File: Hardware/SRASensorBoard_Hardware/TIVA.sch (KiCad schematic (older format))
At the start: 7 parts, among them U4 TM4C129E_Launchpad

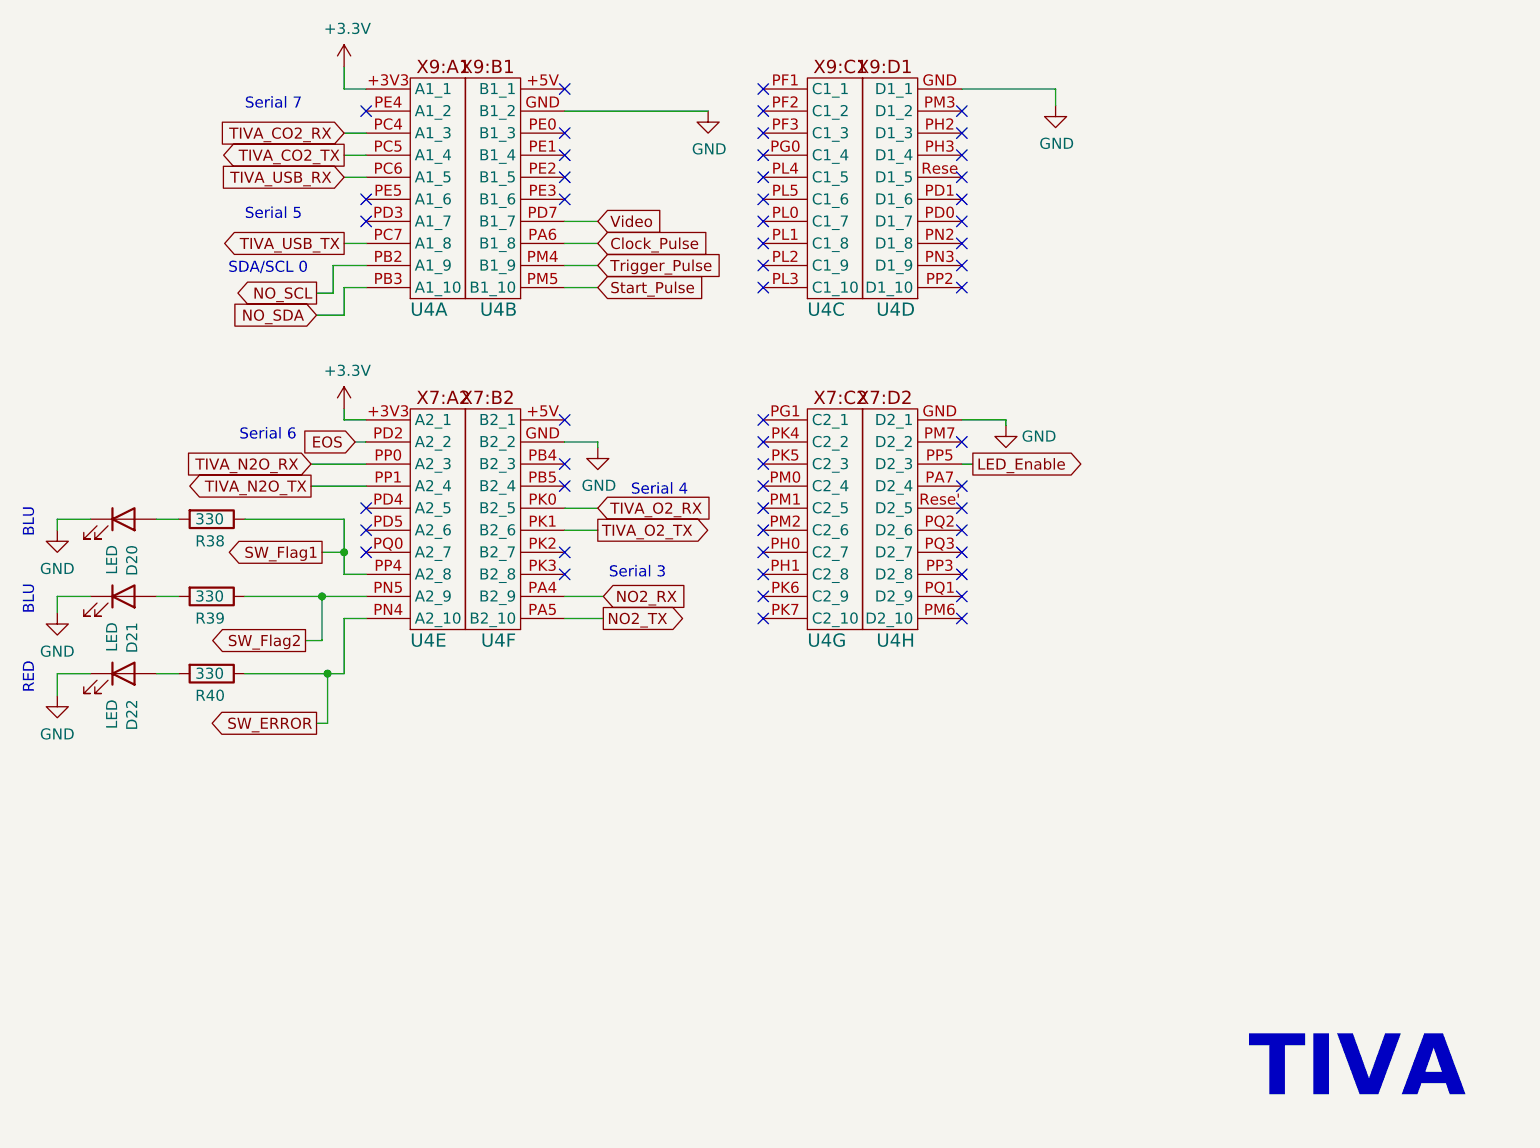
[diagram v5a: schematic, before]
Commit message: Board Progress 3
New mosfets are in but old mosfets need some clean up
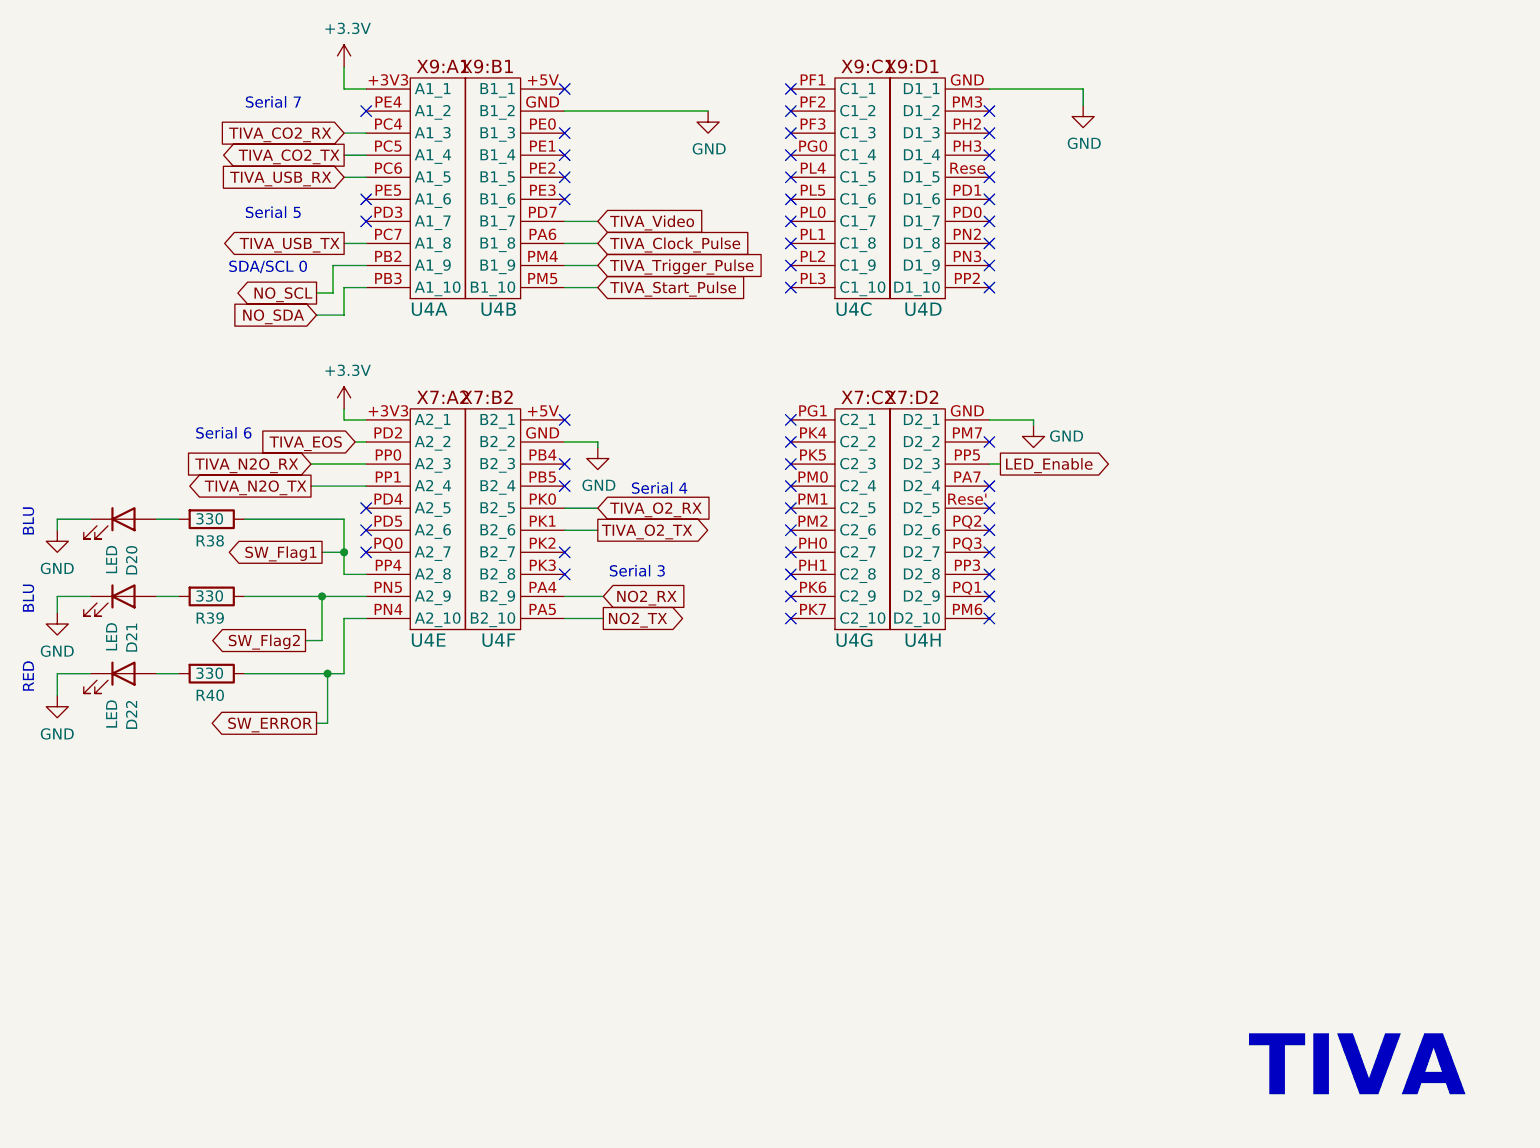
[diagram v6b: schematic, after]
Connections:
- net Clock_Pulse renamed TIVA_Clock_Pulse
- net EOS renamed TIVA_EOS
- net Start_Pulse renamed TIVA_Start_Pulse
- net Trigger_Pulse renamed TIVA_Trigger_Pulse
- net Video renamed TIVA_Video
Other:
- moved on the sheet: U4C, U4D, U4G, U4H
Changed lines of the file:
@@
 TIVA\n
 Wire Wire Line
-	7150 4100 7100 4100
-Text GLabel 7150 4100 2    50   Output ~ 0
+	7275 4100 7225 4100
+Text GLabel 7275 4100 2    50   Output ~ 0
 LED_Enable
 Text GLabel 4175 5275 0    50   Output ~ 0
@@
 L power:GND #PWR0167
 U 1 1 5F933A36
-P 7525 2475
-F 0 "#PWR0167" H 7525 2225 50  0001 C CNN
-F 1 "GND" H 7530 2302 50  0000 C CNN
-F 2 "" H 7525 2475 50  0001 C CNN
-F 3 "" H 7525 2475 50  0001 C CNN
-	1    7525 2475
+P 7650 2475
+F 0 "#PWR0167" H 7650 2225 50  0001 C CNN
+F 1 "GND" H 7655 2302 50  0000 C CNN
+F 2 "" H 7650 2475 50  0001 C CNN
+F 3 "" H 7650 2475 50  0001 C CNN
+	1    7650 2475
 	1    0    0    -1
 $EndComp
@@
 NoConn ~ 5300 4200
 NoConn ~ 5300 4500
-NoConn ~ 6200 4800
-NoConn ~ 6200 4700
-NoConn ~ 6200 4600
-NoConn ~ 6200 4500
-NoConn ~ 6200 4400
-NoConn ~ 6200 4300
-NoConn ~ 6200 4200
-NoConn ~ 6200 4100
-NoConn ~ 7100 4200
-NoConn ~ 7100 4400
-NoConn ~ 7100 4500
-NoConn ~ 7100 4600
-NoConn ~ 7100 4700
-NoConn ~ 7100 4800
-NoConn ~ 7100 3300
-NoConn ~ 7100 3200
-NoConn ~ 7100 3100
-NoConn ~ 7100 3000
-NoConn ~ 7100 2900
-NoConn ~ 7100 2800
-NoConn ~ 7100 2700
-NoConn ~ 7100 2600
-NoConn ~ 6200 2400
-NoConn ~ 6200 2500
-NoConn ~ 6200 2600
-NoConn ~ 6200 2700
-NoConn ~ 6200 2800
-NoConn ~ 6200 2900
-NoConn ~ 6200 3000
-NoConn ~ 6200 3100
-NoConn ~ 6200 3200
-NoConn ~ 6200 3300
+NoConn ~ 6325 4800
+NoConn ~ 6325 4700
+NoConn ~ 6325 4600
+NoConn ~ 6325 4500
+NoConn ~ 6325 4400
+NoConn ~ 6325 4300
+NoConn ~ 6325 4200
+NoConn ~ 6325 4100
+NoConn ~ 7225 4200
+NoConn ~ 7225 4400
+NoConn ~ 7225 4500
+NoConn ~ 7225 4600
+NoConn ~ 7225 4700
+NoConn ~ 7225 4800
+NoConn ~ 7225 3300
+NoConn ~ 7225 3200
+NoConn ~ 7225 3100
+NoConn ~ 7225 3000
+NoConn ~ 7225 2900
+NoConn ~ 7225 2800
+NoConn ~ 7225 2700
+NoConn ~ 7225 2600
+NoConn ~ 6325 2400
+NoConn ~ 6325 2500
+NoConn ~ 6325 2600
+NoConn ~ 6325 2700
+NoConn ~ 6325 2800
+NoConn ~ 6325 2900
+NoConn ~ 6325 3000
+NoConn ~ 6325 3100
+NoConn ~ 6325 3200
+NoConn ~ 6325 3300
 NoConn ~ 4400 3000
 NoConn ~ 4400 2500
 NoConn ~ 5300 2900
-NoConn ~ 7100 4300
+NoConn ~ 7225 4300
 $Comp
 L power:+3.3V #PWR0170
@@
 L SRA_Sensor_Board-rescue:TM4C129E_Launchpad-MRDT_Shields-SRA_Sensor_Board-rescue U4
 U 3 1 5F933A94
-P 6400 3350
-F 0 "U4" H 6400 3300 60  0000 L CNN
-F 1 "TM4C129E_Launchpad" H 6150 3300 60  0001 L CNN
-F 2 "MRDT_Shields:TM4C129E_Launchpad_FULL_SMD_BOTTOM" H 6400 3350 60  0001 C CNN
-F 3 "" H 6400 3350 60  0001 C CNN
-	3    6400 3350
+P 6525 3350
+F 0 "U4" H 6525 3300 60  0000 L CNN
+F 1 "TM4C129E_Launchpad" H 6275 3300 60  0001 L CNN
+F 2 "MRDT_Shields:TM4C129E_Launchpad_FULL_SMD_BOTTOM" H 6525 3350 60  0001 C CNN
+F 3 "" H 6525 3350 60  0001 C CNN
+	3    6525 3350
 	1    0    0    -1
 $EndComp
@@
 L SRA_Sensor_Board-rescue:TM4C129E_Launchpad-MRDT_Shields-SRA_Sensor_Board-rescue U4
 U 8 1 5F933ACF
-P 6900 4850
-F 0 "U4" H 7000 4800 60  0000 C CNN
-F 1 "TM4C129E_Launchpad" H 7150 4800 60  0001 C CNN
-F 2 "MRDT_Shields:TM4C129E_Launchpad_FULL_SMD_BOTTOM" H 6900 4850 60  0001 C CNN
-F 3 "" H 6900 4850 60  0001 C CNN
-	8    6900 4850
+P 7025 4850
+F 0 "U4" H 7125 4800 60  0000 C CNN
+F 1 "TM4C129E_Launchpad" H 7275 4800 60  0001 C CNN
+F 2 "MRDT_Shields:TM4C129E_Launchpad_FULL_SMD_BOTTOM" H 7025 4850 60  0001 C CNN
+F 3 "" H 7025 4850 60  0001 C CNN
+	8    7025 4850
 	-1   0    0    -1
 $EndComp
@@
 L SRA_Sensor_Board-rescue:TM4C129E_Launchpad-MRDT_Shields-SRA_Sensor_Board-rescue U4
 U 7 1 5F933AD5
-P 6400 4850
-F 0 "U4" H 6400 4800 60  0000 L CNN
-F 1 "TM4C129E_Launchpad" H 6150 4800 60  0001 L CNN
-F 2 "MRDT_Shields:TM4C129E_Launchpad_FULL_SMD_BOTTOM" H 6400 4850 60  0001 C CNN
-F 3 "" H 6400 4850 60  0001 C CNN
-	7    6400 4850
-	1    0    0    -1
-$EndComp
-NoConn ~ 7100 4000
-NoConn ~ 6200 3900
-NoConn ~ 6200 4000
+P 6525 4850
+F 0 "U4" H 6525 4800 60  0000 L CNN
+F 1 "TM4C129E_Launchpad" H 6275 4800 60  0001 L CNN
+F 2 "MRDT_Shields:TM4C129E_Launchpad_FULL_SMD_BOTTOM" H 6525 4850 60  0001 C CNN
+F 3 "" H 6525 4850 60  0001 C CNN
+	7    6525 4850
+	1    0    0    -1
+$EndComp
+NoConn ~ 7225 4000
+NoConn ~ 6325 3900
+NoConn ~ 6325 4000
 $Comp
 L power:GND #PWR0171
 U 1 1 5F933ADE
-P 7300 3925
-F 0 "#PWR0171" H 7300 3675 50  0001 C CNN
-F 1 "GND" H 7450 3875 50  0000 C CNN
-F 2 "" H 7300 3925 50  0001 C CNN
-F 3 "" H 7300 3925 50  0001 C CNN
-	1    7300 3925
-	1    0    0    -1
-$EndComp
-Wire Wire Line
-	7300 3900 7100 3900
+P 7425 3925
+F 0 "#PWR0171" H 7425 3675 50  0001 C CNN
+F 1 "GND" H 7575 3875 50  0000 C CNN
+F 2 "" H 7425 3925 50  0001 C CNN
+F 3 "" H 7425 3925 50  0001 C CNN
+	1    7425 3925
+	1    0    0    -1
+$EndComp
+Wire Wire Line
+	7425 3900 7225 3900
 Text Notes 3850 3000 0    50   ~ 0
 Serial 5
@@
 Text GLabel 4150 4200 0    50   Output ~ 0
 TIVA_N2O_TX
-Text Notes 3825 4000 0    50   ~ 0
+Text Notes 3625 4000 0    50   ~ 0
 Serial 6\n
 Wire Wire Line
@@
 $EndComp
 Text GLabel 5450 3000 2    50   Input ~ 0
-Video
+TIVA_Video
 Text GLabel 5450 3100 2    50   Input ~ 0
-Clock_Pulse
+TIVA_Clock_Pulse
 Text GLabel 5450 3200 2    50   Input ~ 0
-Trigger_Pulse
+TIVA_Trigger_Pulse
 Text GLabel 5450 3300 2    50   Input ~ 0
-Start_Pulse
+TIVA_Start_Pulse
 Wire Wire Line
 	5300 3000 5450 3000
@@
 	5300 3300 5450 3300
 Text GLabel 4350 4000 0    50   Input ~ 0
-EOS
+TIVA_EOS
 Wire Wire Line
 	4350 4000 4400 4000
@@
 	3000 5050 3150 5050
 Wire Wire Line
-	7100 2400 7525 2400
-Wire Wire Line
-	7525 2400 7525 2475
+	7225 2400 7650 2400
+Wire Wire Line
+	7650 2400 7650 2475
 Wire Wire Line
 	5450 4000 5450 4025
 Wire Wire Line
-	7300 3900 7300 3925
-NoConn ~ 7100 2500
+	7425 3900 7425 3925
+NoConn ~ 7225 2500
 $Comp
 L SRA_Sensor_Board-rescue:TM4C129E_Launchpad-MRDT_Shields-SRA_Sensor_Board-rescue U4
 U 4 1 5F933A8E
-P 6900 3350
-F 0 "U4" H 7000 3300 60  0000 C CNN
-F 1 "TM4C129E_Launchpad" H 7150 3300 60  0001 C CNN
-F 2 "MRDT_Shields:TM4C129E_Launchpad_FULL_SMD_BOTTOM" H 6900 3350 60  0001 C CNN
-F 3 "" H 6900 3350 60  0001 C CNN
-	4    6900 3350
+P 7025 3350
+F 0 "U4" H 7125 3300 60  0000 C CNN
+F 1 "TM4C129E_Launchpad" H 7275 3300 60  0001 C CNN
+F 2 "MRDT_Shields:TM4C129E_Launchpad_FULL_SMD_BOTTOM" H 7025 3350 60  0001 C CNN
+F 3 "" H 7025 3350 60  0001 C CNN
+	4    7025 3350
 	-1   0    0    -1
 $EndComp

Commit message: Board Progress 7 (final rev 1)
Final edits for REV 1
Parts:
- added D1, D2, D23, D3, D4: LED, Diode_SMD:D_0603_1608Metric_Pad1.05x0.95mm_HandSolder, symbol Device:LED
- added R49, R50, R51, R52, R53: 330, Resistor_SMD:R_0603_1608Metric_Pad1.05x0.95mm_HandSolder, symbol Device:R
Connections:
- net GND: now also D1.1 (K), D2.1 (K), D23.1 (K), D3.1 (K), D4.1 (K)
- net TIVA_Clock_Pulse: now also R51.1
- net TIVA_EOS: now also R49.1
- net TIVA_Start_Pulse: now also R53.1
- net TIVA_Trigger_Pulse: now also R52.1
- net TIVA_Video: now also R50.1
- new net: D2.2 (A), R50.2
- new net: D3.2 (A), R51.2
- new net: D4.2 (A), R52.2
- new net: D23.2 (A), R53.2
- new net: D1.2 (A), R49.2
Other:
- moved on the sheet: U4C, U4D, U4G, U4H

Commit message: Fixed some library issues
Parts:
- R38, R39, R40, R49, R50, R51, R52, R53: value 330 -> 480; footprint Resistor_SMD:R_0603_1608Metric_Pad1.05x0.95mm_HandSolder -> Resistor_SMD:R_0603_1608Metric_Pad0.98x0.95mm_HandSolder
- U4: symbol SRA_Sensor_Board-rescue:TM4C129E_Launchpad-MRDT_Shields-SRA_Sensor_Board-rescue -> MRDT_Shields:TM4C129E_Launchpad
- U4: symbol SRA_Sensor_Board-rescue:TM4C129E_Launchpad-MRDT_Shields -> MRDT_Shields:TM4C129E_Launchpad
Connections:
- net +3V3: now also U4.+3V3' (A2_1); no longer U4.+3V3 (A2_1)
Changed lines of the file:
@@
 EESchema Schematic File Version 4
+LIBS:SRA_Sensor_Board-cache
 EELAYER 30 0
 EELAYER END
@@
 NoConn ~ 4400 2900
 $Comp
-L SRA_Sensor_Board-rescue:TM4C129E_Launchpad-MRDT_Shields-SRA_Sensor_Board-rescue U4
+L MRDT_Shields:TM4C129E_Launchpad U4
 U 3 1 5F933A94
 P 6850 3350
+AR Path="/5F933A94" Ref="U4"  Part="3"
+AR Path="/5F8FEC08/5F933A94" Ref="U4"  Part="3"
 F 0 "U4" H 6850 3300 60  0000 L CNN
 F 1 "TM4C129E_Launchpad" H 6600 3300 60  0001 L CNN
@@
 $EndComp
 $Comp
-L SRA_Sensor_Board-rescue:TM4C129E_Launchpad-MRDT_Shields-SRA_Sensor_Board-rescue U4
+L MRDT_Shields:TM4C129E_Launchpad U4
 U 1 1 5F933AA0
 P 4600 3350
+AR Path="/5F933AA0" Ref="U4"  Part="1"
+AR Path="/5F8FEC08/5F933AA0" Ref="U4"  Part="1"
 F 0 "U4" H 4600 3300 60  0000 L CNN
 F 1 "TM4C129E_Launchpad" H 4350 3300 60  0001 L CNN
@@
 	4300 3900 4400 3900
 $Comp
-L SRA_Sensor_Board-rescue:TM4C129E_Launchpad-MRDT_Shields U4
+L MRDT_Shields:TM4C129E_Launchpad U4
 U 5 1 5F933AAE
 P 4600 4850
+AR Path="/5F933AAE" Ref="U4"  Part="5"
+AR Path="/5F8FEC08/5F933AAE" Ref="U4"  Part="5"
 F 0 "U4" H 4600 4800 60  0000 L CNN
 F 1 "TM4C129E_Launchpad" H 4400 4800 60  0001 L CNN
@@
 $EndComp
 $Comp
-L SRA_Sensor_Board-rescue:TM4C129E_Launchpad-MRDT_Shields U4
+L MRDT_Shields:TM4C129E_Launchpad U4
 U 6 1 5F933AB4
 P 5100 4850
+AR Path="/5F933AB4" Ref="U4"  Part="6"
+AR Path="/5F8FEC08/5F933AB4" Ref="U4"  Part="6"
 F 0 "U4" H 5200 4800 60  0000 C CNN
 F 1 "TM4C129E_Launchpad" H 5300 4800 60  0001 C CNN
@@
 $EndComp
 $Comp
-L SRA_Sensor_Board-rescue:TM4C129E_Launchpad-MRDT_Shields-SRA_Sensor_Board-rescue U4
+L MRDT_Shields:TM4C129E_Launchpad U4
 U 8 1 5F933ACF
 P 7350 4850
+AR Path="/5F933ACF" Ref="U4"  Part="8"
+AR Path="/5F8FEC08/5F933ACF" Ref="U4"  Part="8"
 F 0 "U4" H 7450 4800 60  0000 C CNN
 F 1 "TM4C129E_Launchpad" H 7600 4800 60  0001 C CNN
@@
 $EndComp
 $Comp
-L SRA_Sensor_Board-rescue:TM4C129E_Launchpad-MRDT_Shields-SRA_Sensor_Board-rescue U4
+L MRDT_Shields:TM4C129E_Launchpad U4
 U 7 1 5F933AD5
 P 6850 4850
+AR Path="/5F933AD5" Ref="U4"  Part="7"
+AR Path="/5F8FEC08/5F933AD5" Ref="U4"  Part="7"
 F 0 "U4" H 6850 4800 60  0000 L CNN
 F 1 "TM4C129E_Launchpad" H 6600 4800 60  0001 L CNN
@@
 AR Path="/5F8FEC08/605279B4" Ref="R40"  Part="1"
 F 0 "R40" V 3800 4975 50  0000 L CNN
-F 1 "330" V 3700 4975 50  0000 L CNN
-F 2 "Resistor_SMD:R_0603_1608Metric_Pad1.05x0.95mm_HandSolder" V 3630 5050 50  0001 C CNN
+F 1 "480" V 3700 4975 50  0000 L CNN
+F 2 "Resistor_SMD:R_0603_1608Metric_Pad0.98x0.95mm_HandSolder" V 3630 5050 50  0001 C CNN
 F 3 "~" H 3700 5050 50  0001 C CNN
 	1    3700 5050
@@
 AR Path="/5F8FEC08/605279C4" Ref="R38"  Part="1"
 F 0 "R38" V 3800 4275 50  0000 L CNN
-F 1 "330" V 3700 4275 50  0000 L CNN
-F 2 "Resistor_SMD:R_0603_1608Metric_Pad1.05x0.95mm_HandSolder" V 3630 4350 50  0001 C CNN
+F 1 "480" V 3700 4275 50  0000 L CNN
+F 2 "Resistor_SMD:R_0603_1608Metric_Pad0.98x0.95mm_HandSolder" V 3630 4350 50  0001 C CNN
 F 3 "~" H 3700 4350 50  0001 C CNN
 	1    3700 4350
@@
 AR Path="/5F8FEC08/605279D4" Ref="R39"  Part="1"
 F 0 "R39" V 3800 4625 50  0000 L CNN
-F 1 "330" V 3700 4625 50  0000 L CNN
-F 2 "Resistor_SMD:R_0603_1608Metric_Pad1.05x0.95mm_HandSolder" V 3630 4700 50  0001 C CNN
+F 1 "480" V 3700 4625 50  0000 L CNN
+F 2 "Resistor_SMD:R_0603_1608Metric_Pad0.98x0.95mm_HandSolder" V 3630 4700 50  0001 C CNN
 F 3 "~" H 3700 4700 50  0001 C CNN
 	1    3700 4700
@@
 NoConn ~ 5300 3900
 $Comp
-L SRA_Sensor_Board-rescue:TM4C129E_Launchpad-MRDT_Shields-SRA_Sensor_Board-rescue U4
+L MRDT_Shields:TM4C129E_Launchpad U4
 U 2 1 5F933A9A
 P 5100 3350
+AR Path="/5F933A9A" Ref="U4"  Part="2"
+AR Path="/5F8FEC08/5F933A9A" Ref="U4"  Part="2"
 F 0 "U4" H 5200 3300 60  0000 C CNN
 F 1 "TM4C129E_Launchpad" H 5350 3300 60  0001 C CNN
@@
 NoConn ~ 7550 2500
 $Comp
-L SRA_Sensor_Board-rescue:TM4C129E_Launchpad-MRDT_Shields-SRA_Sensor_Board-rescue U4
+L MRDT_Shields:TM4C129E_Launchpad U4
 U 4 1 5F933A8E
 P 7350 3350
+AR Path="/5F933A8E" Ref="U4"  Part="4"
+AR Path="/5F8FEC08/5F933A8E" Ref="U4"  Part="4"
 F 0 "U4" H 7450 3300 60  0000 C CNN
 F 1 "TM4C129E_Launchpad" H 7600 3300 60  0001 C CNN
@@
 AR Path="/5F8FEC08/60AEE3A6" Ref="R50"  Part="1"
 F 0 "R50" V 5575 2425 50  0000 L CNN
-F 1 "330" V 5625 2575 50  0000 L CNN
-F 2 "Resistor_SMD:R_0603_1608Metric_Pad1.05x0.95mm_HandSolder" V 5555 2650 50  0001 C CNN
+F 1 "480" V 5625 2575 50  0000 L CNN
+F 2 "Resistor_SMD:R_0603_1608Metric_Pad0.98x0.95mm_HandSolder" V 5555 2650 50  0001 C CNN
 F 3 "~" H 5625 2650 50  0001 C CNN
 	1    5625 2650
@@
 AR Path="/5F8FEC08/60CF753B" Ref="R51"  Part="1"
 F 0 "R51" V 5575 2675 50  0000 L CNN
-F 1 "330" V 5625 2825 50  0000 L CNN
-F 2 "Resistor_SMD:R_0603_1608Metric_Pad1.05x0.95mm_HandSolder" V 5555 2900 50  0001 C CNN
+F 1 "480" V 5625 2825 50  0000 L CNN
+F 2 "Resistor_SMD:R_0603_1608Metric_Pad0.98x0.95mm_HandSolder" V 5555 2900 50  0001 C CNN
 F 3 "~" H 5625 2900 50  0001 C CNN
 	1    5625 2900
@@
 AR Path="/5F8FEC08/60D6145F" Ref="R52"  Part="1"
 F 0 "R52" V 5600 2975 50  0000 L CNN
-F 1 "330" V 5650 3100 50  0000 L CNN
-F 2 "Resistor_SMD:R_0603_1608Metric_Pad1.05x0.95mm_HandSolder" V 5580 3175 50  0001 C CNN
+F 1 "480" V 5650 3100 50  0000 L CNN
+F 2 "Resistor_SMD:R_0603_1608Metric_Pad0.98x0.95mm_HandSolder" V 5580 3175 50  0001 C CNN
 F 3 "~" H 5650 3175 50  0001 C CNN
 	1    5650 3175
@@
 AR Path="/5F8FEC08/60E141A4" Ref="R53"  Part="1"
 F 0 "R53" V 5600 3225 50  0000 L CNN
-F 1 "330" V 5650 3350 50  0000 L CNN
-F 2 "Resistor_SMD:R_0603_1608Metric_Pad1.05x0.95mm_HandSolder" V 5580 3425 50  0001 C CNN
+F 1 "480" V 5650 3350 50  0000 L CNN
+F 2 "Resistor_SMD:R_0603_1608Metric_Pad0.98x0.95mm_HandSolder" V 5580 3425 50  0001 C CNN
 F 3 "~" H 5650 3425 50  0001 C CNN
 	1    5650 3425
@@
 AR Path="/5F8FEC08/60EBE8EC" Ref="R49"  Part="1"
 F 0 "R49" V 3950 3725 50  0000 L CNN
-F 1 "330" V 4000 3850 50  0000 L CNN
-F 2 "Resistor_SMD:R_0603_1608Metric_Pad1.05x0.95mm_HandSolder" V 3930 3925 50  0001 C CNN
+F 1 "480" V 4000 3850 50  0000 L CNN
+F 2 "Resistor_SMD:R_0603_1608Metric_Pad0.98x0.95mm_HandSolder" V 3930 3925 50  0001 C CNN
 F 3 "~" H 4000 3925 50  0001 C CNN
 	1    4000 3925
